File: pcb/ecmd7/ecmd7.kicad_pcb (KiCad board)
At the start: 2 copper layers, 120 x 90 mm, 181 parts, among them J1 PMOD_SPI_ENC, J2 PMOD_ADC_MPIO, J3 PMOD_DRV, J4 Conn_01x02_Socket, J5 Encoder, J7 RS422/BISS-C, Q1 IRFS3806, Q2 IRFS3806, Q3 IRFS3806, Q4 IRFS3806, Q5 IRFS3806, Q6 IRFS3806, Q7 BSC098N10NS5, Q8 BSC098N10NS5, U1 TMC6200-TA, U10 FIN1002M5X, U11 FIN1002M5X, U12 FIN1002M5X, U13 ADM3490ExR, U2 MCP33151-05T-E/MN, U3 LM5118MH, U4 MCP33151-05T-E/MN, U5 MCP33151-05T-E/MN, U6 TLV71318PDBV, U7 MCP33151-05T-E/MN, U8 LT1616ES6#TRPBF, U9 LT1616ES6#TRPBF

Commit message: Initial component placement
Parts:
- removed C11: 100n, Capacitor_SMD:C_0805_2012Metric
- removed C12: 1u, Capacitor_SMD:C_0805_2012Metric
- removed L3: 10u, Inductor_SMD:L_TechFuse_SL0530
- removed U8: LT1616ES6#TRPBF, Package_TO_SOT_SMD:SOT-23-6
- added C61: 100n, Capacitor_SMD:C_0805_2012Metric, F.Cu at (71.5, 55.5)
- added C62: 100n, Capacitor_SMD:C_0805_2012Metric, F.Cu at (88.5, 64.0)
- added C63: 100n, Capacitor_SMD:C_0805_2012Metric, F.Cu at (71.5, 63.5)
- added C64: 100n, Capacitor_SMD:C_0805_2012Metric, F.Cu at (71.5, 61.5)
- added C65: 6.8n, Capacitor_SMD:C_0805_2012Metric, F.Cu at (71.5, 71.5)
- added C66: 220p, Capacitor_SMD:C_0805_2012Metric, F.Cu at (73.0, 68.5)
- added C67: 100n, Capacitor_SMD:C_0805_2012Metric, F.Cu at (89.5, 61.0)
- added C68: 470n, Capacitor_SMD:C_0805_2012Metric, F.Cu at (82.5, 71.5)
- added C69: 470n, Capacitor_SMD:C_0805_2012Metric, F.Cu at (79.5, 71.5)
- added C70: 330u, Capacitor_SMD:CP_Elec_6.3x9.9, F.Cu at (80.0, 77.5)
- added D14: SK220ATR, Diode_SMD:D_SMA, F.Cu at (92.0, 57.5)
- added D15: SK220ATR, Diode_SMD:D_SMA, F.Cu at (92.0, 53.5)
- added D16: SK220ATR, Diode_SMD:D_SMA, F.Cu at (89.0, 73.5)
- added D17: SK220ATR, Diode_SMD:D_SMA, F.Cu at (89.0, 77.5)
- added D18: 3.3V, Diode_SMD:D_0805_2012Metric, F.Cu at (116.5, 122.5)
- added D19: DRV_EN, Diode_SMD:D_0805_2012Metric, F.Cu at (100.5, 126.0)
- added D20: DRV_EN, Diode_SMD:D_0805_2012Metric, F.Cu at (109.5, 126.0)
- added H1: GND, MountingHole:MountingHole_3.2mm_M3_Pad_Via, F.Cu at (65.0, 45.0)
- added H2: GND, MountingHole:MountingHole_3.2mm_M3_Pad_Via, F.Cu at (65.0, 125.0)
- added H3: PGND, MountingHole:MountingHole_3.2mm_M3_Pad_Via, F.Cu at (175.0, 45.0)
- added H4: PGND, MountingHole:MountingHole_3.2mm_M3_Pad_Via, F.Cu at (175.0, 125.0)
- added J6: 12V, Connector_PinHeader_2.00mm:PinHeader_1x02_P2.00mm_Vertical, F.Cu at (122.0, 124.0)
- added J8: 5V, Connector_PinHeader_2.00mm:PinHeader_1x02_P2.00mm_Vertical, F.Cu at (122.0, 121.0)
- added JP9: SolderJumper_2_Open, Jumper:SolderJumper-2_P1.3mm_Open_RoundedPad1.0x1.5mm, F.Cu at (102.0, 84.0)
- added L6: 10u, Inductor_SMD:L_TechFuse_SL0530, F.Cu at (94.0, 62.5)
- added NT1: NetTie_2, NetTie:NetTie-2_SMD_Pad0.5mm, F.Cu at (168.0, 68.0)
- added NT10: NetTie_2, NetTie:NetTie-2_SMD_Pad2.0mm, B.Cu at (150.0, 54.0)
- added NT2: NetTie_2, NetTie:NetTie-2_SMD_Pad0.5mm, F.Cu at (168.0, 88.0)
- added NT3: NetTie_2, NetTie:NetTie-2_SMD_Pad0.5mm, F.Cu at (168.0, 108.0)
- added NT4: NetTie_2, NetTie:NetTie-2_SMD_Pad0.5mm, F.Cu at (144.0, 71.0)
- added NT5: NetTie_2, NetTie:NetTie-2_SMD_Pad0.5mm, F.Cu at (144.0, 91.0)
- added NT6: NetTie_2, NetTie:NetTie-2_SMD_Pad0.5mm, F.Cu at (144.0, 111.0)
- added NT7: NetTie_2, NetTie:NetTie-2_SMD_Pad2.0mm, B.Cu at (150.0, 59.0)
- added NT8: NetTie_2, NetTie:NetTie-2_SMD_Pad2.0mm, B.Cu at (150.0, 79.0)
- added NT9: NetTie_2, NetTie:NetTie-2_SMD_Pad2.0mm, B.Cu at (150.0, 99.0)
- added Q10: BSC098N10NS5, Package_TO_SOT_SMD:TDSON-8-1, F.Cu at (92.0, 68.5)
- added Q11: MMBT3904, Package_TO_SOT_SMD:SOT-23, F.Cu at (97.5, 126.0)
- added Q12: MMBT3904, Package_TO_SOT_SMD:SOT-23, F.Cu at (106.5, 126.0)
- added Q9: BSC098N10NS5, Package_TO_SOT_SMD:TDSON-8-1, F.Cu at (88.5, 48.5)
- added R44: 62k, Resistor_SMD:R_0805_2012Metric, F.Cu at (75.0, 53.5)
- added R45: 15k, Resistor_SMD:R_0805_2012Metric, F.Cu at (71.5, 53.5)
- added R65: 1M, Resistor_SMD:R_0805_2012Metric, F.Cu at (71.5, 59.5)
- added R66: 18k, Resistor_SMD:R_0805_2012Metric, F.Cu at (71.5, 57.5)
- added R67: 15k, Resistor_SMD:R_0805_2012Metric, F.Cu at (71.0, 68.5)
- added R68: 1k, Resistor_SMD:R_0805_2012Metric, F.Cu at (71.5, 65.5)
- added R69: 4.7k, Resistor_SMD:R_0805_2012Metric, F.Cu at (97.5, 123.0)
- added R70: 3k, Resistor_SMD:R_0805_2012Metric, F.Cu at (75.0, 71.5)
- added R71: 15m, Resistor_SMD:R_0612_1632Metric, F.Cu at (86.5, 53.5)
- added R72: 330, Resistor_SMD:R_0805_2012Metric, F.Cu at (100.5, 122.5)
- added R73: 4.7k, Resistor_SMD:R_0805_2012Metric, F.Cu at (106.5, 123.0)
- added R74: 330, Resistor_SMD:R_0805_2012Metric, F.Cu at (109.5, 122.5)
- added R75: 470, Resistor_SMD:R_0805_2012Metric, F.Cu at (96.0, 119.5)
- added TP1: GND, TestPoint:TestPoint_Loop_D2.50mm_Drill1.0mm, F.Cu at (72.0, 45.0)
- added TP2: PGND, TestPoint:TestPoint_Loop_D2.50mm_Drill1.0mm, F.Cu at (168.0, 125.0)
- added U14: LM5118MH, Package_SO:Texas_PWP0020A, F.Cu at (80.5, 62.0)
- C35: value 15n -> 8.2n
- C36: value 180p -> 100p
- D5: value MBR0530 -> 12V; footprint Diode_SMD:D_SOD-123 -> Diode_SMD:D_0805_2012Metric
- D6: value D -> 5V; footprint Diode_SMD:D_MiniMELF -> Diode_SMD:D_0805_2012Metric
- JU1, JV1, JW1: footprint MountingHole:MountingHole_3.2mm_M3_Pad_TopBottom -> MountingHole:MountingHole_3.2mm_M3_Pad_Via
- R15: footprint Resistor_SMD:R_0805_2012Metric -> Resistor_SMD:R_0612_1632Metric
- R19: value 27k -> 36k
- R31: value 4k7 -> 470
- R46: value 470 -> 4.7k
- R47: value 32k -> 1.5k
- R48: value 10k -> 470
- R9: value 1 -> 0.47
- moved U12 322.4 mm to (75.5, 125.0), turned to 90 degrees
- moved R42 320.8 mm to (78.5, 125.0), turned to -90 degrees
- moved C56 320.6 mm to (72.5, 127.0), turned to -90 degrees
- moved U11 320.1 mm to (75.5, 117.0), turned to 90 degrees
- moved R41 320.0 mm to (80.5, 123.0), turned to -90 degrees
- moved C52 319.6 mm to (72.5, 119.0), turned to -90 degrees
- moved R43 318.3 mm to (80.5, 126.5), turned to -90 degrees
- moved U10 318.2 mm to (75.5, 109.5), turned to 90 degrees
- moved C51 317.3 mm to (72.5, 111.5), turned to -90 degrees
- moved U6 314.3 mm to (98.5, 95.0), turned to -90 degrees
- moved R36 309.9 mm to (78.5, 117.0), turned to -90 degrees
- moved R35 309.5 mm to (80.5, 115.5), turned to -90 degrees
- moved D5 307.4 mm to (121.0, 127.0)
- moved D6 306.7 mm to (121.0, 118.0)
- moved R34 306.0 mm to (80.5, 107.5), turned to -90 degrees
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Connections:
- C13 pad 2: 0 -> GNDPWR
- C14 pad 2: 0 -> GNDPWR
- C15 pad 2: 0 -> GNDPWR
- C16 pad 2: 0 -> GNDPWR
- C17 pad 2: 0 -> GNDPWR
- C18 pad 2: 0 -> GNDPWR
- C26 pad 1: Net-(U1-USENSE) -> Net-(U1-U)
- C27 pad 1: Net-(Q3-S) -> Net-(U1-V)
- C28 pad 1: Net-(Q5-S) -> Net-(U1-W)
- C50 pad 1: +3V3_IO -> +3.3V
- C58 pad 1: /ADC + I/O/A_LS_P -> /ADC+IO/A_LS_P
- C59 pad 1: /ADC + I/O/A_LS_P -> /ADC+IO/B_LS_P
- C60 pad 1: /ADC + I/O/A_LS_P -> /ADC+IO/Z_LS_P
- C7 pad 1: +3V3_IO -> +3.3V
- C8 pad 1: +3V3_IO -> +3.3V
- C9 pad 1: +3V3_IO -> +3.3V
- D10 pad 1: /ADC + I/O/A_LS_N -> /ADC+IO/B_LS_N
- D10 pad 2: /ADC + I/O/A_LS_P -> /ADC+IO/B_LS_P
- D11 pad 1: /ADC + I/O/A_LS_N -> /ADC+IO/Z_LS_N
- D11 pad 2: /ADC + I/O/A_LS_P -> /ADC+IO/Z_LS_P
- D12 pad 1: RS422_TX_A -> RS422_TX_B
- D12 pad 2: RS422_TX_B -> RS422_TX_A
- D5 pad 1: Net-(D5-K) -> 0
- D5 pad 2: 0 -> Net-(D5-A)
- D6 pad 1: Net-(D6-K) -> 0
- D6 pad 2: +5V -> Net-(D6-A)
- D9 pad 1: /ADC + I/O/A_LS_N -> /ADC+IO/A_LS_N
- D9 pad 2: /ADC + I/O/A_LS_P -> /ADC+IO/A_LS_P
- J4 pad 2: 0 -> GNDPWR
- JP3 pad 1: +3.3V_IO -> +12V
- JP8 pad 2: +12V -> +3.3V_IO
- Q2 pad 3: 0 -> GNDPWR
- Q4 pad 3: 0 -> GNDPWR
- Q6 pad 3: 0 -> GNDPWR
- R10 pad 2: Net-(JU1-Pin_1) -> Net-(NT1-Pad2)
- R22 pad 2: /ADC + I/O/A_LS_N -> /ADC+IO/A_LS_N
- R23 pad 2: /ADC + I/O/A_LS_P -> /ADC+IO/A_LS_P
- R24 pad 2: /ADC + I/O/A_LS_N -> /ADC+IO/B_LS_N
- R25 pad 2: /ADC + I/O/A_LS_P -> /ADC+IO/B_LS_P
- R29 pad 2: +3V3 -> +3.3V
- R31 pad 1: AD_SDO_IU -> AD_SCK
- R31 pad 2: +3V3 -> +3.3V
- R32 pad 1: /ADC + I/O/A_LS_P -> /ADC+IO/A_LS_P
- R33 pad 1: /ADC + I/O/A_LS_N -> /ADC+IO/A_LS_N
- R33 pad 2: /ADC + I/O/A_LS_P -> /ADC+IO/A_LS_P
- R34 pad 2: /ADC + I/O/A_LS_N -> /ADC+IO/A_LS_N
- R35 pad 2: /ADC + I/O/A_LS_N -> /ADC+IO/B_LS_N
- R36 pad 1: /ADC + I/O/A_LS_N -> /ADC+IO/B_LS_N
- R36 pad 2: /ADC + I/O/A_LS_P -> /ADC+IO/B_LS_P
- R38 pad 1: /ADC + I/O/A_LS_P -> /ADC+IO/B_LS_P
- R39 pad 2: /ADC + I/O/A_LS_N -> /ADC+IO/Z_LS_N
- R40 pad 2: /ADC + I/O/A_LS_P -> /ADC+IO/Z_LS_P
- R41 pad 2: /ADC + I/O/A_LS_N -> /ADC+IO/Z_LS_N
- R42 pad 1: /ADC + I/O/A_LS_N -> /ADC+IO/Z_LS_N
- R42 pad 2: /ADC + I/O/A_LS_P -> /ADC+IO/Z_LS_P
- R43 pad 1: /ADC + I/O/A_LS_P -> /ADC+IO/Z_LS_P
- R46 pad 1: +12V -> Net-(D5-A)
- R46 pad 2: Net-(U8-~{SHDN}) -> +12V
- R47 pad 1: Net-(U8-FB) -> Net-(D6-A)
- R48 pad 1: Net-(U8-FB) -> Net-(D18-A)
- R48 pad 2: 0 -> +3.3V
- R5 pad 2: Net-(JV1-Pin_1) -> Net-(NT2-Pad1)
- R50 pad 1: Net-(JP8-A) -> Net-(JP3-B)
- R50 pad 2: Net-(JP3-B) -> Net-(JP8-A)
- R55 pad 1: /ADC + I/O/A_LS_N -> /ADC+IO/B_LS_N
- R56 pad 2: /ADC + I/O/A_LS_P -> /ADC+IO/B_LS_P
- R57 pad 2: /ADC + I/O/A_LS_P -> /ADC+IO/Z_LS_P
- R58 pad 1: /ADC + I/O/A_LS_N -> /ADC+IO/Z_LS_N
- R59 pad 2: /ADC + I/O/A_LS_P -> /ADC+IO/A_LS_P
- R60 pad 1: /ADC + I/O/A_LS_N -> /ADC+IO/A_LS_N
- R61 pad 1: /ADC + I/O/A_LS_N -> /ADC+IO/A_LS_N
- R62 pad 1: /ADC + I/O/A_LS_N -> /ADC+IO/B_LS_N
- R63 pad 1: /ADC + I/O/A_LS_N -> /ADC+IO/Z_LS_N
- R64 pad 2: Net-(JP3-B) -> Net-(JP8-A)
- R8 pad 2: Net-(JW1-Pin_1) -> Net-(NT3-Pad1)
- U1 pad 38: Net-(Q5-S) -> Net-(U1-W)
- U1 pad 42: Net-(Q3-S) -> Net-(U1-V)
- U1 pad 47: Net-(Q1-S) -> Net-(U1-U)
- U10 pad 3: /ADC + I/O/A_LS_P -> /ADC+IO/A_LS_P
- U10 pad 4: /ADC + I/O/A_LS_N -> /ADC+IO/A_LS_N
- U11 pad 3: /ADC + I/O/A_LS_P -> /ADC+IO/B_LS_P
- U11 pad 4: /ADC + I/O/A_LS_N -> /ADC+IO/B_LS_N
- U12 pad 3: /ADC + I/O/A_LS_P -> /ADC+IO/Z_LS_P
- U12 pad 4: /ADC + I/O/A_LS_N -> /ADC+IO/Z_LS_N
- U2 pad 10: +3V3 -> +3.3V
- U4 pad 10: +3V3 -> +3.3V
- U5 pad 10: +3V3 -> +3.3V
- U7 pad 10: +3V3 -> +3.3V
- U9 pad 4: Net-(JP3-B) -> Net-(JP8-A)

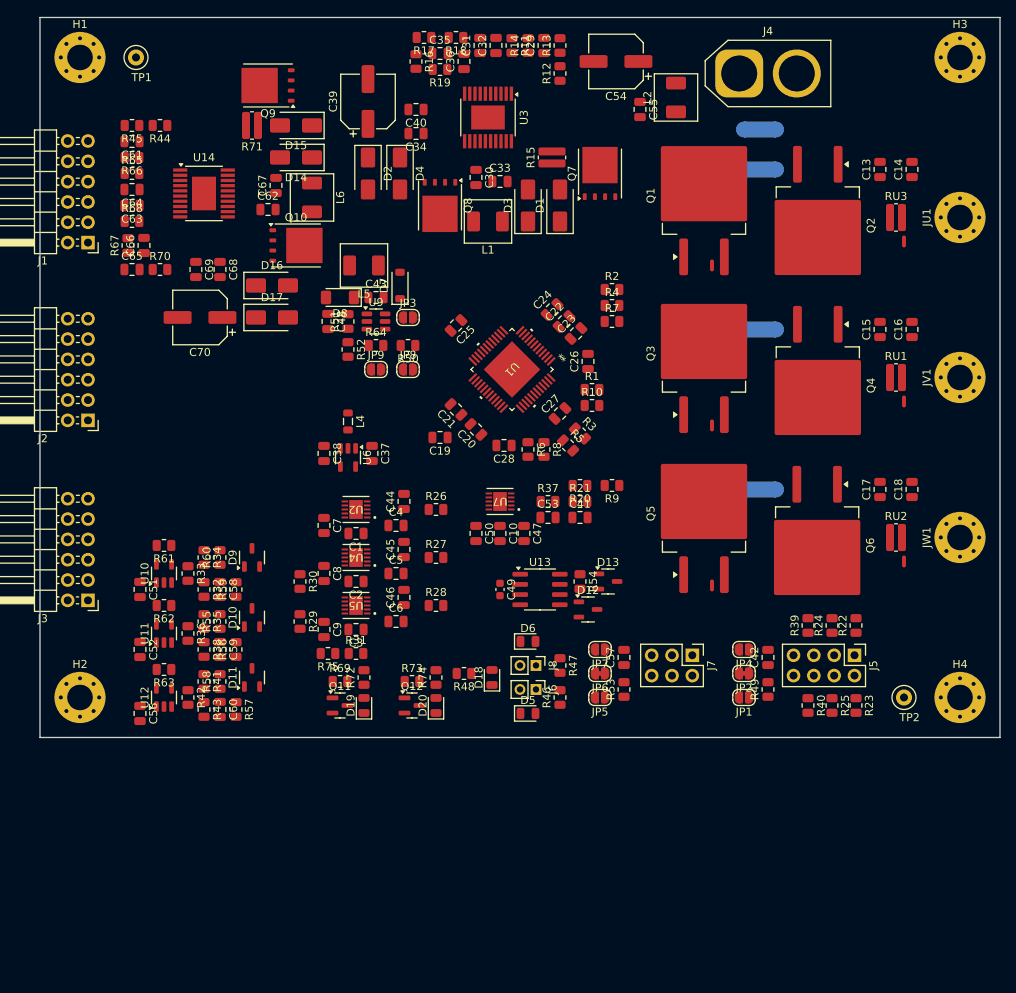
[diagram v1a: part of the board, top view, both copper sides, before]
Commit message: WIP: Update symbols, fix ERC errors
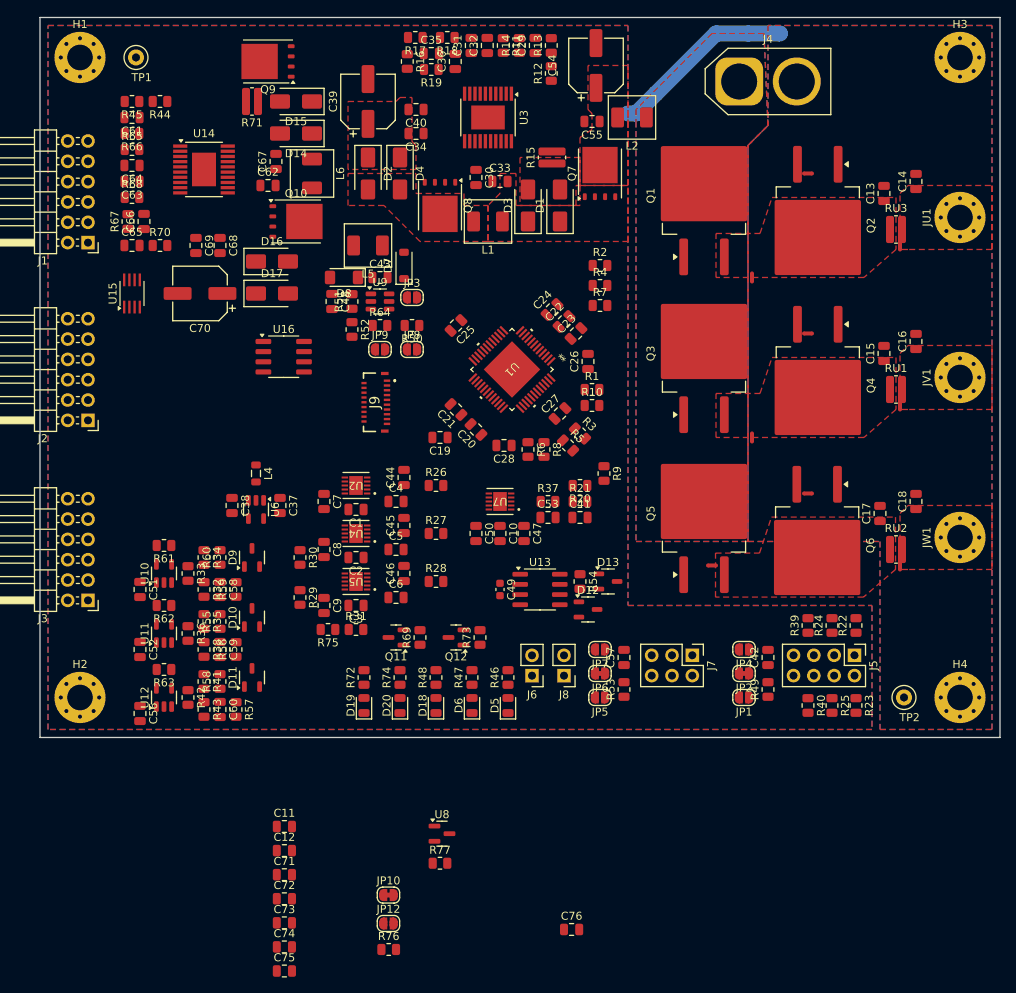
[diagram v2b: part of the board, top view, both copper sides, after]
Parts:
- removed NT1, NT2, NT3, NT4, NT5, NT6: NetTie_2, NetTie:NetTie-2_SMD_Pad0.5mm
- removed NT7, NT8, NT9: NetTie_2, NetTie:NetTie-2_SMD_Pad2.0mm
- added C11: 1u, Capacitor_SMD:C_0805_2012Metric, F.Cu at (90.5, 141.1)
- added C12: 1u, Capacitor_SMD:C_0805_2012Metric, F.Cu at (90.5, 144.1)
- added C71: 100n, Capacitor_SMD:C_0805_2012Metric, F.Cu at (90.5, 147.2)
- added C72: 10u, Capacitor_SMD:C_0805_2012Metric, F.Cu at (90.5, 150.2)
- added C73: 10u, Capacitor_SMD:C_0805_2012Metric, F.Cu at (90.5, 153.2)
- added C74: 100n, Capacitor_SMD:C_0805_2012Metric, F.Cu at (90.5, 156.2)
- added C75: 100n, Capacitor_SMD:C_0805_2012Metric, F.Cu at (90.5, 159.2)
- added C76: 100n, Capacitor_SMD:C_0805_2012Metric, F.Cu at (126.5, 154.0)
- added J9: FH35C-19S-0.3SHW_99_, SSTA:FH35C19S03SHW99, F.Cu at (101.8, 88.1)
- added JP10: SolderJumper_2_Bridged, Jumper:SolderJumper-2_P1.3mm_Bridged_RoundedPad1.0x1.5mm, F.Cu at (103.6, 149.7)
- added JP12: SolderJumper_2_Open, Jumper:SolderJumper-2_P1.3mm_Open_RoundedPad1.0x1.5mm, F.Cu at (103.6, 153.2)
- added NTGU1: NetTie_2, NetTie:NetTie-2_SMD_Pad0.5mm, F.Cu at (156.0, 59.5)
- added NTGV1: NetTie_2, NetTie:NetTie-2_SMD_Pad0.5mm, F.Cu at (156.0, 79.5)
- added NTGW1: NetTie_2, NetTie:NetTie-2_SMD_Pad0.5mm, F.Cu at (156.0, 99.5)
- added NTPU1: NetTie_2, NetTie:NetTie-2_SMD_Pad0.5mm, F.Cu at (149.0, 72.5)
- added NTPV1: NetTie_2, NetTie:NetTie-2_SMD_Pad0.5mm, F.Cu at (149.0, 92.5)
- added NTPW1: NetTie_2, NetTie:NetTie-2_SMD_Pad0.5mm, F.Cu at (144.0, 108.5)
- added NTSU1: NetTie_2, NetTie:NetTie-2_SMD_Pad0.5mm, F.Cu at (167.5, 68.5)
- added NTSV1: NetTie_2, NetTie:NetTie-2_SMD_Pad0.5mm, F.Cu at (167.5, 88.5)
- added NTSW1: NetTie_2, NetTie:NetTie-2_SMD_Pad0.5mm, F.Cu at (167.5, 108.5)
- added R76: 10k, Resistor_SMD:R_0805_2012Metric, F.Cu at (103.6, 156.5)
- added R77: 10k, Resistor_SMD:R_0805_2012Metric, F.Cu at (110.0, 145.7)
- added U15: 74LVC1G139, Package_SO:SSOP-8_2.95x2.8mm_P0.65mm, F.Cu at (71.5, 74.5)
- added U16: MB85RS1MT, Package_SO:SOP-8_3.76x4.96mm_P1.27mm, F.Cu at (90.5, 82.4)
- added U8: TLV803EA30DBZ, Package_TO_SOT_SMD:SOT-23, F.Cu at (110.2, 142.0)
- D20: value DRV_EN -> FAULT
- J6, J8: footprint Connector_PinHeader_2.00mm:PinHeader_1x02_P2.00mm_Vertical -> Connector_PinHeader_2.54mm:PinHeader_1x02_P2.54mm_Vertical
- U1: footprint sst_footprints:eTQFP48_9x9_TRI -> SSTA:eTQFP48_9x9_TRI
- U2, U4, U5, U7: footprint sst_footprints:TDFN10_MN_MCH -> SSTA:TDFN10_MN_MCH
- moved C37 13.2 mm to (90.0, 101.0)
- moved C38 13.2 mm to (84.0, 101.0)
- moved L4 13.2 mm to (87.0, 97.0)
- moved U6 13.2 mm to (87.0, 101.5)
- moved NTP2G1 12.0 mm to (150.5, 42.0)
- moved R69 11.4 mm to (107.5, 117.5), turned to 90 degrees
- moved R47 11.1 mm to (114.0, 122.5), turned to 90 degrees
- moved Q11 11.0 mm to (104.5, 117.5), turned to 180 degrees
- moved D6 10.6 mm to (114.0, 126.0), turned to 90 degrees
- moved Q12 10.1 mm to (112.0, 117.5), turned to 180 degrees
- moved R73 10.1 mm to (115.0, 117.5), turned to 90 degrees
- moved D18 7.83 mm to (109.5, 126.0)
- moved R46 6.96 mm to (118.5, 122.5)
- moved C55 6.18 mm to (129.0, 53.0), turned to 180 degrees
- moved L2 6.04 mm to (134.0, 52.5), turned to 180 degrees
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- renumbered NT10 to NTP2G1
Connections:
- net 0 renamed GND
- C24 pad 1: +5V -> +5VA
- C37 pad 1: +5VA -> Net-(U6-EN)
- C38 pad 1: +5VA -> Net-(U6-EN)
- J1 pad 10: /CS_DRV -> /CS_0
- J1 pad 7: /CS_EXT -> /CS_1
- L4 pad 2: +5VA -> Net-(U6-EN)
- U1 pad 7: +5V -> +5VA
- U6 pad 1: +5VA -> Net-(U6-EN)
- U6 pad 3: +5VA -> Net-(U6-EN)
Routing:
- net GND: track 0.00 -> 19.1 mm
- added copper zone on F.Cu, net +12V
- added copper zone on B.Cu, net GND
- added copper zone on F.Cu, net GND
- added copper zone on In1.Cu, net GND
- added copper zone on In2.Cu, net GND
- added copper zone on B.Cu, net GNDPWR
- added copper zone on F.Cu, net GNDPWR
- added copper zone on F.Cu, net Net-(D1-A)
- added copper zone on F.Cu, net Net-(D1-K)
- added copper zone on F.Cu, net Net-(D2-A)
- added copper zone on F.Cu, net Net-(JU1-Pin_1)
- added copper zone on F.Cu, net Net-(JV1-Pin_1)
- added copper zone on F.Cu, net Net-(JW1-Pin_1)
- added copper zone on F.Cu, net Net-(Q1-S)
- added copper zone on F.Cu, net Net-(Q3-S)
- added copper zone on F.Cu, net Net-(Q5-S)
- added copper zone on B.Cu, net VMot
- added copper zone on F.Cu, net VMot
- added copper zone on F.Cu, net VSupply
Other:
- copper layers 2 -> 4

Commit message: WIP: Power stage and ADC routing
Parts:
- added D21: SMAJ60A, Diode_SMD:D_SMA, F.Cu at (151.0, 53.5)
- added J10: SPI Ext., Connector_PinSocket_2.54mm:PinSocket_1x06_P2.54mm_Vertical, F.Cu at (79.5, 140.3)
- added NTPV2: NetTie_2, NetTie:NetTie-2_SMD_Pad0.5mm, F.Cu at (121.5, 76.4)
- added NTPW3: NetTie_2, NetTie:NetTie-2_SMD_Pad0.5mm, B.Cu at (134.5, 100.1)
- moved R9 29.2 mm to (134.0, 68.0), turned to 0 degrees
- moved R28 13.5 mm to (109.0, 97.0), turned to -90 degrees
- moved C1 12.9 mm to (102.5, 114.0)
- moved C3 12.9 mm to (102.5, 101.0)
- moved C4 12.9 mm to (107.5, 113.0)
- moved C6 12.9 mm to (107.5, 100.0)
- moved C7 12.9 mm to (98.5, 113.0)
- moved C9 12.9 mm to (98.5, 101.0)
- moved U2 12.9 mm to (102.5, 111.0)
- moved U5 12.9 mm to (102.5, 98.0)
- moved C44 12.5 mm to (106.5, 110.0)
- moved C46 12.5 mm to (106.5, 97.0)
- moved R26 11.5 mm to (109.0, 110.0), turned to -90 degrees
- moved R20 7.38 mm to (134.0, 102.0)
- moved NTPW1 5.28 mm to (149.0, 106.8), turned to 90 degrees
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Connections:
- C41 pad 2: GND -> VMOT_REF
- C44 pad 2: GND -> I_REF
- C45 pad 2: GND -> I_REF
- C46 pad 2: GND -> I_REF
- C53 pad 2: GND -> VMOT_REF
- R21 pad 2: GND -> VMOT_REF
- U15 pad 7: unconnected-(U15-Y0-Pad7) -> /CS_EXT
- U2 pad 4: GND -> I_REF
- U4 pad 4: GND -> I_REF
- U5 pad 4: GND -> I_REF
- U7 pad 4: GND -> VMOT_REF
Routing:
- net GND: track 19.1 -> 119.7 mm, vias 0 -> 10
- net Net-(NTSW1-Pad1): track 0.00 -> 49.6 mm, vias 0 -> 2
- net Net-(NTSV1-Pad1): track 0.00 -> 44.5 mm, vias 0 -> 2
- net Net-(NTSU1-Pad2): track 0.00 -> 44.3 mm, vias 0 -> 2
- net Net-(Q6-G): track 0.00 -> 41.2 mm, vias 0 -> 2
- net I_U: track 0.00 -> 39.5 mm, vias 0 -> 2
- net Net-(U1-W): track 0.00 -> 39.1 mm, vias 0 -> 2
- net Net-(Q2-G): track 0.00 -> 35.1 mm, vias 0 -> 2
- net I_V: track 0.00 -> 33.3 mm, vias 0 -> 2
- net Net-(Q4-G): track 0.00 -> 31.8 mm, vias 0 -> 2
- net Net-(U1-V): track 0.00 -> 31.6 mm, vias 0 -> 2
- net Net-(U1-U): track 0.00 -> 31.4 mm, vias 0 -> 2
- net Net-(Q5-G): track 0.00 -> 29.5 mm, vias 0 -> 2
- net I_W: track 0.00 -> 24.8 mm, vias 0 -> 2
- net Net-(Q1-G): track 0.00 -> 24.5 mm, vias 0 -> 2
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- added copper zone on F.Cu, net +5V
- added copper zone on B.Cu, net I_REF
- added copper zone on In1.Cu, net I_REF
- added copper zone on In2.Cu, net I_REF
- added copper zone on F.Cu, net Net-(D14-K)
- added copper zone on F.Cu, net Net-(D16-A)
- added copper zone on B.Cu, net VMOT_REF
- added copper zone on B.Cu, net VSupply
